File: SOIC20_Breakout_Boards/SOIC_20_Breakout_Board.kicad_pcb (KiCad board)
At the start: 2 copper layers, 25 x 25 mm, 6 parts, among them J1 Conn_01x04, J2 Conn_01x04, J3 Conn_01x01, J4 Conn_01x01

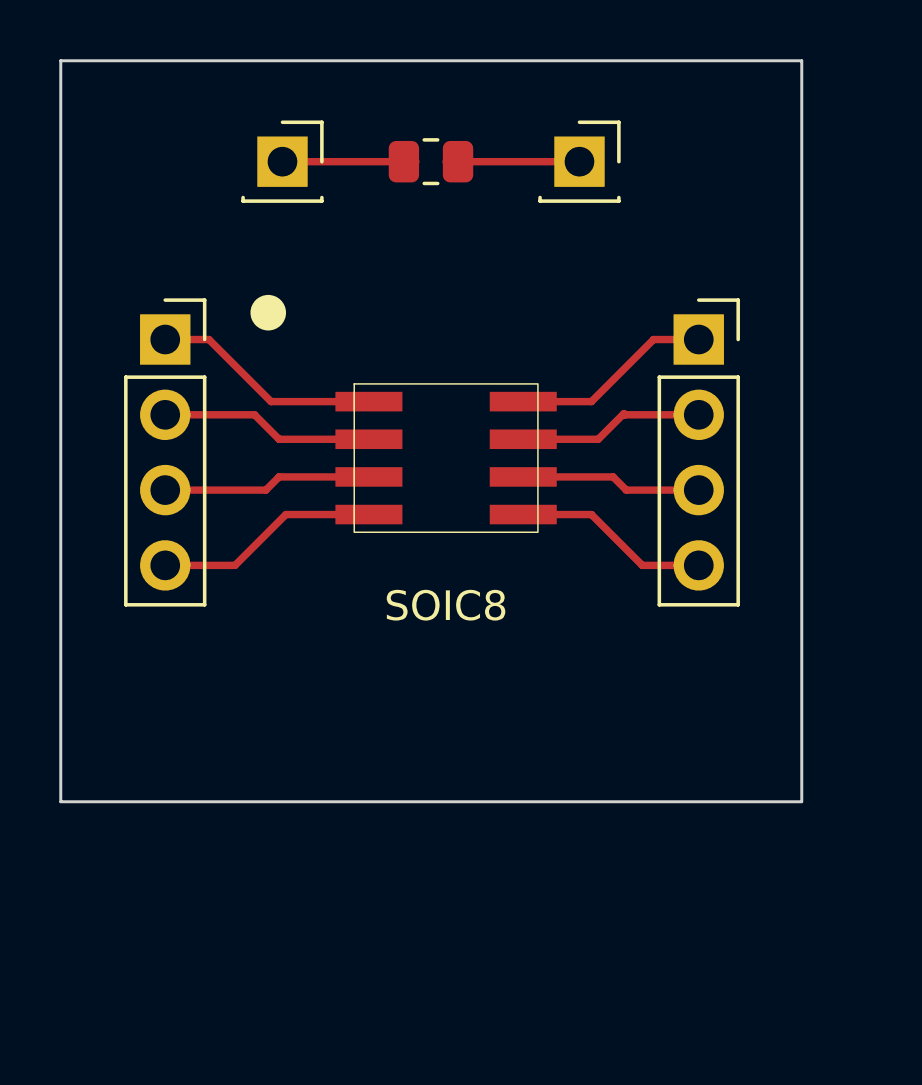
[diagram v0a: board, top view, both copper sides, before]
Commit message: Created PCB designs for the 14, 16 & 20 pic SOIC's
Finalized and committed pcb designs for the 14, 16, and 20 SOIC breakout boards
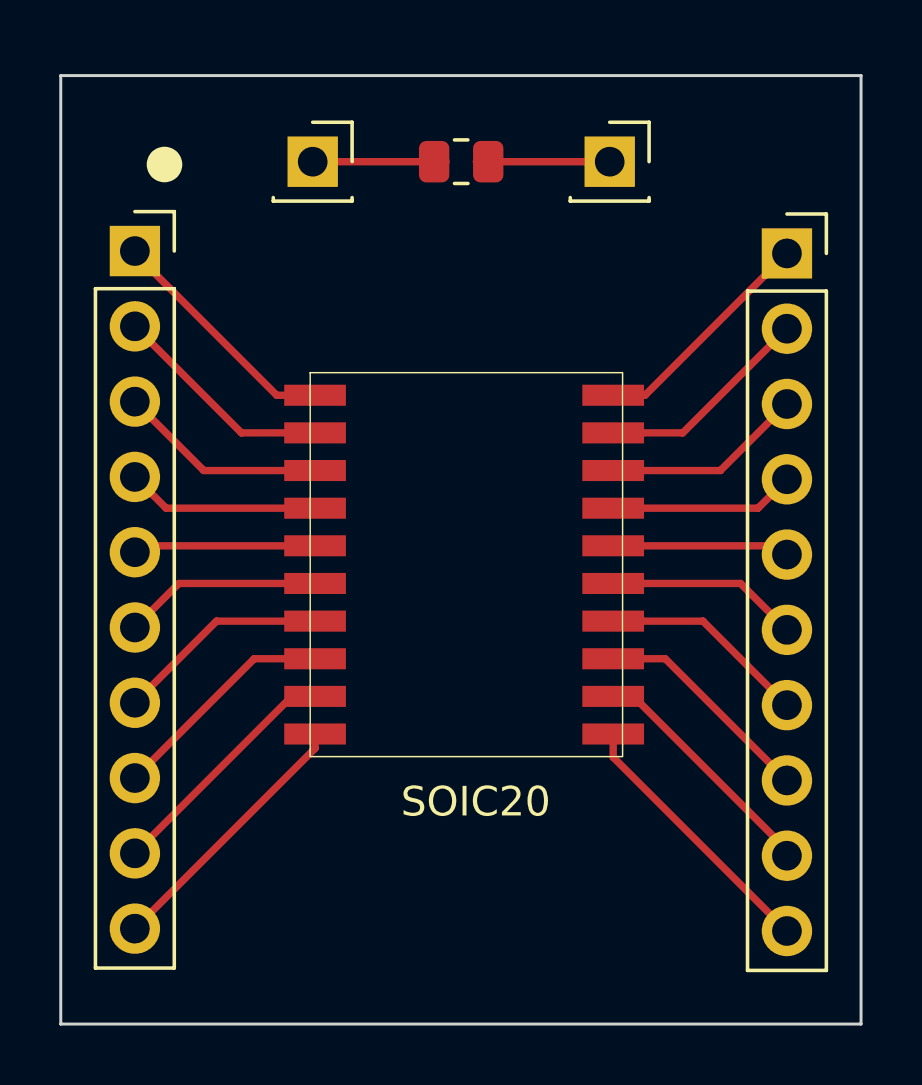
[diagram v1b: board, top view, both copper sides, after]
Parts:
- removed SOIC8: 8_Pin_SOIC_Board, SOIC_Footprints:8_Pin_SOIC_Board
- added SOIC20: 20_Pin_SOIC_Board, SOIC_Footprints:20_Pin_SOIC_Board, F.Cu at (156.3, 105.0)
- J1, J2: value Conn_01x04 -> Conn_01x10; footprint Connector_PinSocket_2.54mm:PinSocket_1x04_P2.54mm_Vertical -> Connector_PinSocket_2.54mm:PinSocket_1x10_P2.54mm_Vertical
- moved J2 4.16 mm to (166.5, 94.5)
- moved J1 3.16 mm to (144.5, 94.4)
- moved J3 1.02 mm to (160.5, 91.4)
- moved J4 1.02 mm to (150.5, 91.4)
- moved R1 1.02 mm to (155.5, 91.4)
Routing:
- net Net-(J1-Pad10): track 0.00 -> 9.08 mm
- net Net-(J2-Pad10): track 0.00 -> 9.07 mm
- net Net-(J2-Pad9): track 0.00 -> 9.01 mm
- net Net-(J1-Pad9): track 0.00 -> 8.27 mm
- net Net-(J1-Pad8): track 0.00 -> 7.75 mm
- net Net-(J2-Pad8): track 0.00 -> 7.56 mm
- net Net-(J1-Pad7): track 0.00 -> 7.22 mm
- net Net-(J2-Pad7): track 0.00 -> 7.04 mm
- net Net-(J1-Pad6): track 0.00 -> 6.69 mm
- net Net-(J2-Pad6): track 0.00 -> 6.51 mm
- net Net-(J1-Pad5): track 0.00 -> 6.17 mm
- net Net-(J2-Pad5): track 0.00 -> 5.98 mm
- net Net-(J1-Pad1): track 7.24 -> 8.14 mm
- net Net-(J2-Pad4): track 7.13 -> 6.27 mm
- net Net-(J1-Pad2): track 6.71 -> 7.57 mm
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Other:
- board size 25 x 25 mm -> 27 x 32 mm
- board text added: "20 Pin SOIC Breakout Board"
- board text removed: "8 Pin SOIC Breakout Board"

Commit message: Fixed warnings on all SOIC boards
Ensured that silkscreen traces didn't intersect solder masks and name/board information is visible on the front of the board rather than the back
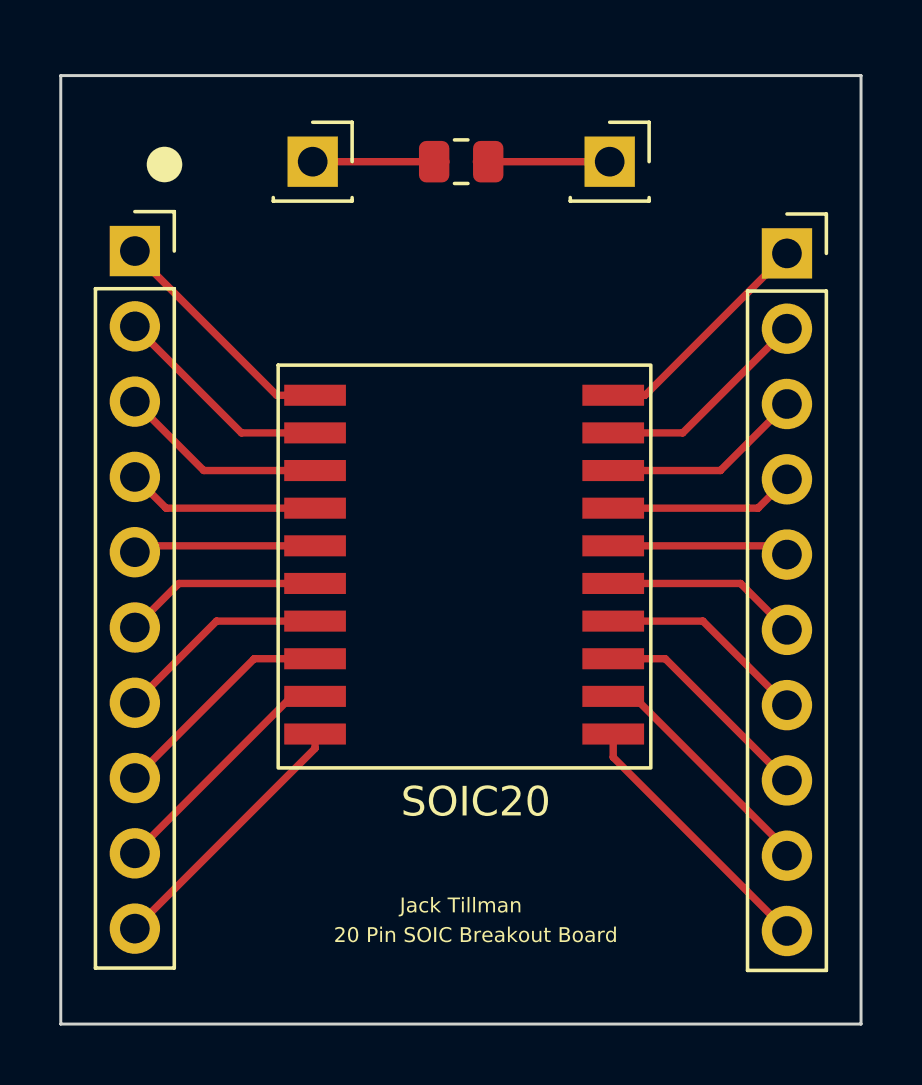
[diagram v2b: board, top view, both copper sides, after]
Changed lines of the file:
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@@
       (effects (font (size 1 1) (thickness 0.15)))
     )
-    (fp_rect (start -5.9055 -6.477) (end 4.6355 6.477) (layer "F.SilkS") (width 0.05) (fill none))
-    (fp_rect (start -6.985 -6.731) (end 5.588 6.858) (layer "F.Fab") (width 0.12) (fill none))
+    (fp_rect (start -6.985 -6.731) (end 5.588 6.858) (layer "F.SilkS") (width 0.12) (fill none))
+    (fp_rect (start -5.9055 -6.477) (end 4.6355 6.477) (layer "F.Fab") (width 0.05) (fill none))
     (pad "1" smd rect (at -5.7404 -5.715) (size 2.0828 0.7112) (layers "F.Cu" "F.Paste" "F.Mask")
       (net 1 "Net-(J1-Pad1)") (pintype "unspecified"))
@@
   (gr_circle (center 145.5 91.5) (end 146 91.5) (layer "F.SilkS") (width 0.2) (fill solid))
   (gr_rect (start 142 88.5) (end 169 120.5) (layer "Edge.Cuts") (width 0.1) (fill none))
-  (gr_text "20 Pin SOIC Breakout Board" (at 156 117.5) (layer "B.SilkS")
+  (gr_text "20 Pin SOIC Breakout Board" (at 156 117.5) (layer "F.SilkS")
     (effects (font (size 0.5 0.5) (thickness 0.05)))
   )
-  (gr_text "Jack Tillman" (at 155 116.5) (layer "B.SilkS")
+  (gr_text "Jack Tillman" (at 155.5 116.5) (layer "F.SilkS")
     (effects (font (size 0.5 0.5) (thickness 0.05)))
   )

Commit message: Finished tracing the SOIC20 board
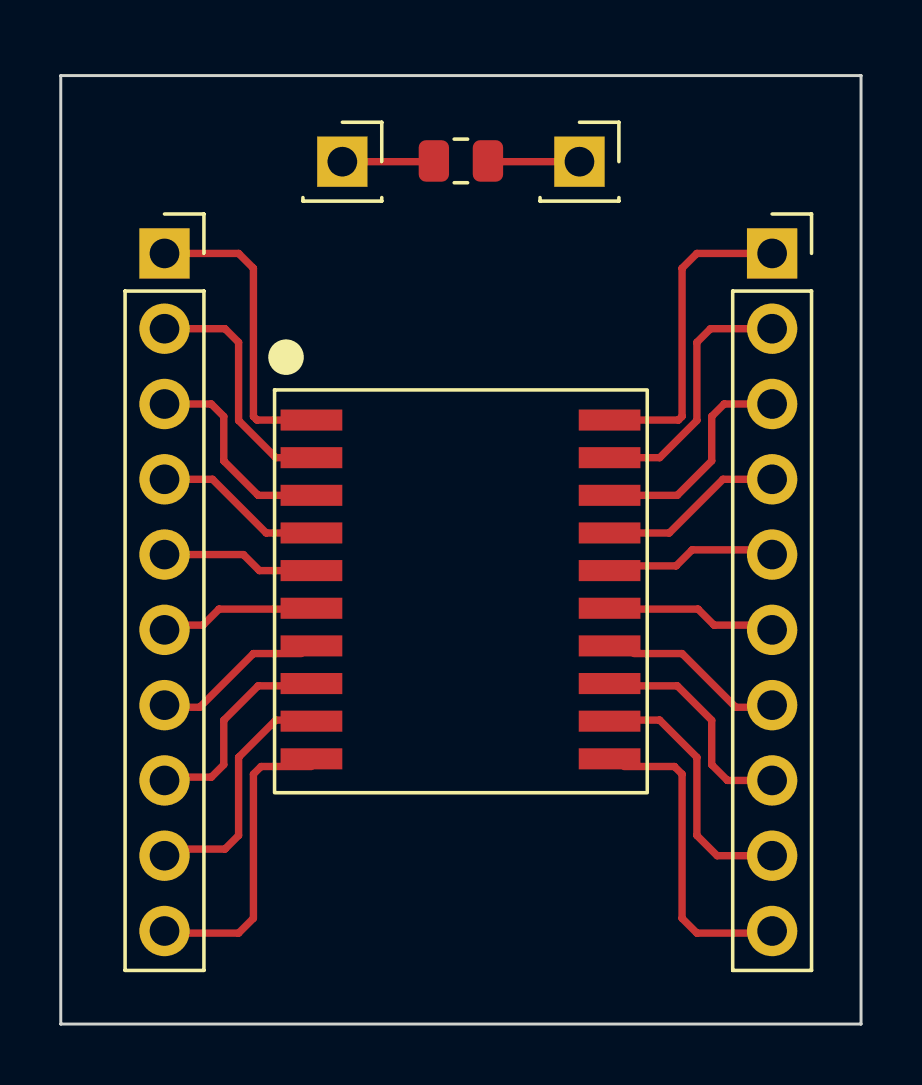
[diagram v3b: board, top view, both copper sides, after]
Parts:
- moved J3 1.02 mm to (159.5, 91.4)
- moved J1 1.00 mm to (145.5, 94.5)
- moved J4 1.00 mm to (151.5, 91.4)
- moved SOIC20 0.85 mm to (156.2, 105.8)
- moved J2 0.50 mm to (166.0, 94.5)
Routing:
- net Net-(J2-Pad1): track 7.84 -> 10.2 mm
- net Net-(J1-Pad1): track 8.14 -> 10.2 mm
- net Net-(J1-Pad6): track 6.69 -> 5.18 mm
- net Net-(J1-Pad7): track 7.22 -> 5.71 mm
- net Net-(J4-Pad1): track 4.50 -> 3.10 mm
- net Net-(J2-Pad6): track 6.51 -> 5.18 mm
- net Net-(J2-Pad7): track 7.04 -> 5.71 mm
- net Net-(J2-Pad10): track 9.07 -> 10.1 mm
- net Net-(J1-Pad10): track 9.08 -> 10.1 mm
- net Net-(J2-Pad2): track 7.32 -> 8.30 mm
- net Net-(J1-Pad5): track 6.17 -> 5.18 mm
- net Net-(J3-Pad1): track 3.98 -> 3.10 mm
- net Net-(J1-Pad4): track 6.52 -> 5.71 mm
- net Net-(J1-Pad2): track 7.57 -> 8.30 mm
- net Net-(J2-Pad5): track 5.98 -> 5.29 mm
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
